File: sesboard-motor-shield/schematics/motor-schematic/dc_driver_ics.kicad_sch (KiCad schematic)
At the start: 0 parts

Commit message: added servo power supply
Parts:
- added J2: EXTERNAL_MOTOR_POWER, symbol Connector:Screw_Terminal_01x02
- added J3: MOTOR_C_OUT, symbol Connector:Screw_Terminal_01x02
- added J4: MOTOR_D_OUT, symbol Connector:Screw_Terminal_01x02
- added J5: MOTOR_A_OUT, symbol Connector:Screw_Terminal_01x02
- added J6: MOTOR_B_OUT, symbol Connector:Screw_Terminal_01x02
- added U2, U3: L293D, Package_DIP:DIP-16_W7.62mm, symbol Driver_Motor:L293D
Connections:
- new net +5V: U2.16 (VCC1), U3.16 (VCC1)
- new net ENA: U3.1 (EN1,2)
- new net ENB: U3.9 (EN3,4)
- new net ENC: U2.1 (EN1,2)
- new net END: U2.9 (EN3,4)
- new net GND: J2.1 (Pin_1), U2.12 (GND), U2.13 (GND), U2.4 (GND), U2.5 (GND), U3.12 (GND), U3.13 (GND), U3.4 (GND), U3.5 (GND)
- new net IN1: U3.2 (1A)
- new net IN2: U3.7 (2A)
- new net IN3: U3.10 (3A)
- new net IN4: U3.15 (4A)
- new net IN5: U2.2 (1A)
- new net IN6: U2.7 (2A)
- new net IN7: U2.10 (3A)
- new net IN8: U2.15 (4A)
- new net MOTOR_A_OUT+: J5.1 (Pin_1), U3.3 (1Y)
- new net MOTOR_A_OUT-: J5.2 (Pin_2), U3.6 (2Y)
- new net MOTOR_B_OUT-: J6.1 (Pin_1), J6.2 (Pin_2), U3.11 (3Y), U3.14 (4Y)
- new net MOTOR_C_OUT+: J3.1 (Pin_1), U2.3 (1Y)
- new net MOTOR_C_OUT-: J3.2 (Pin_2), U2.6 (2Y)
- new net MOTOR_D_OUT-: J4.1 (Pin_1), U2.11 (3Y), U2.14 (4Y)
- new net MOTOR_EXT+: J2.2 (Pin_2), U2.8 (VCC2), U3.8 (VCC2)
- new net MOTOR_d_OUT-: J4.2 (Pin_2)
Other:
- note added: "*a total of 4 DC motors can be controlled by these 2 ICs *a total of 2 stepper motors can be controlled by these 2 ICs"
- note added: "MOTOR DRIVERS"

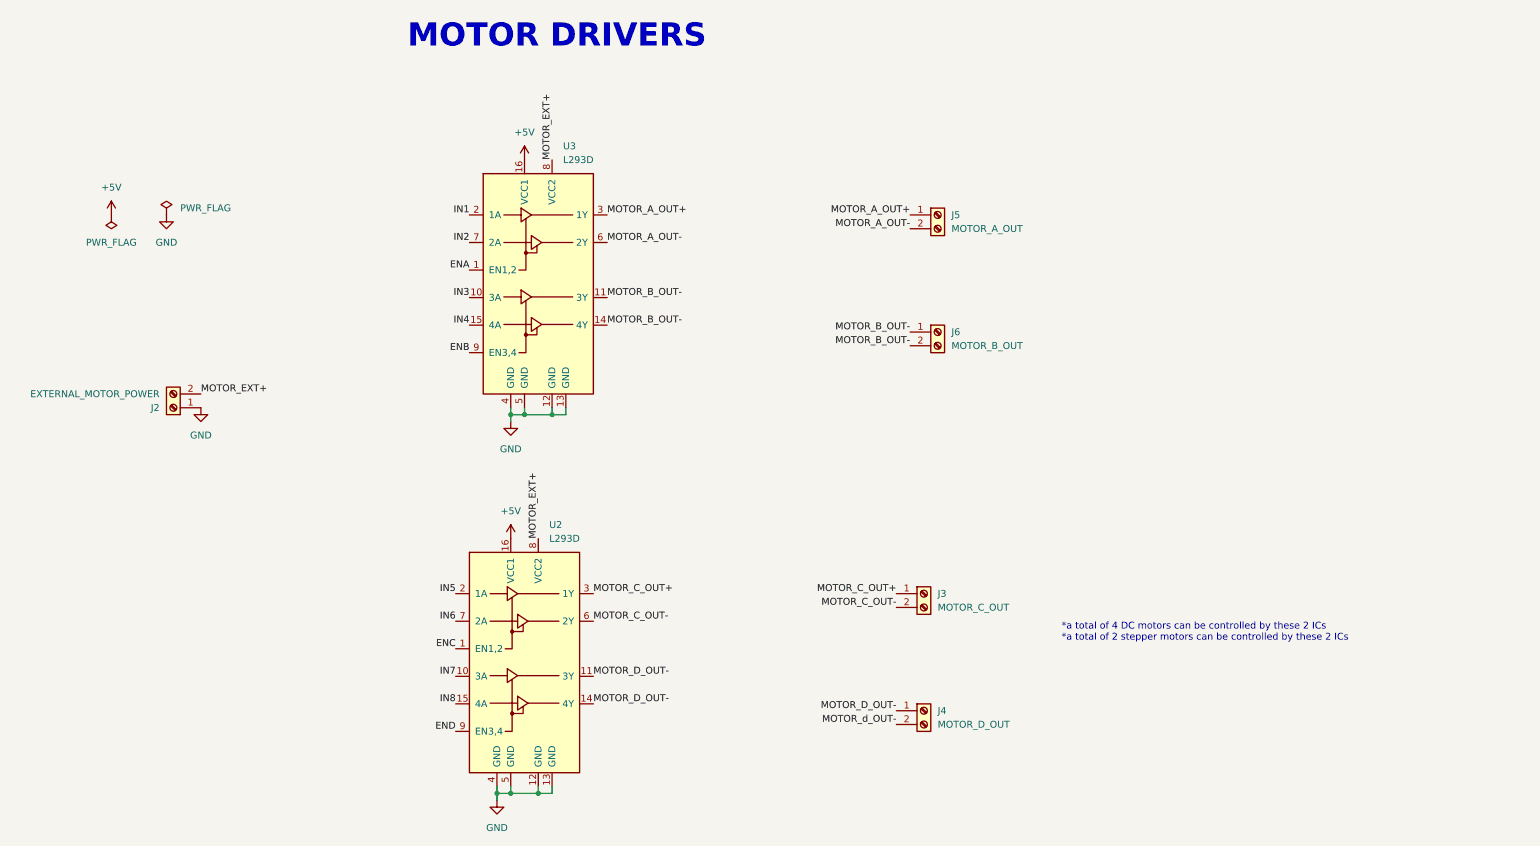
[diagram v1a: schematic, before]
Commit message: added pin assignments
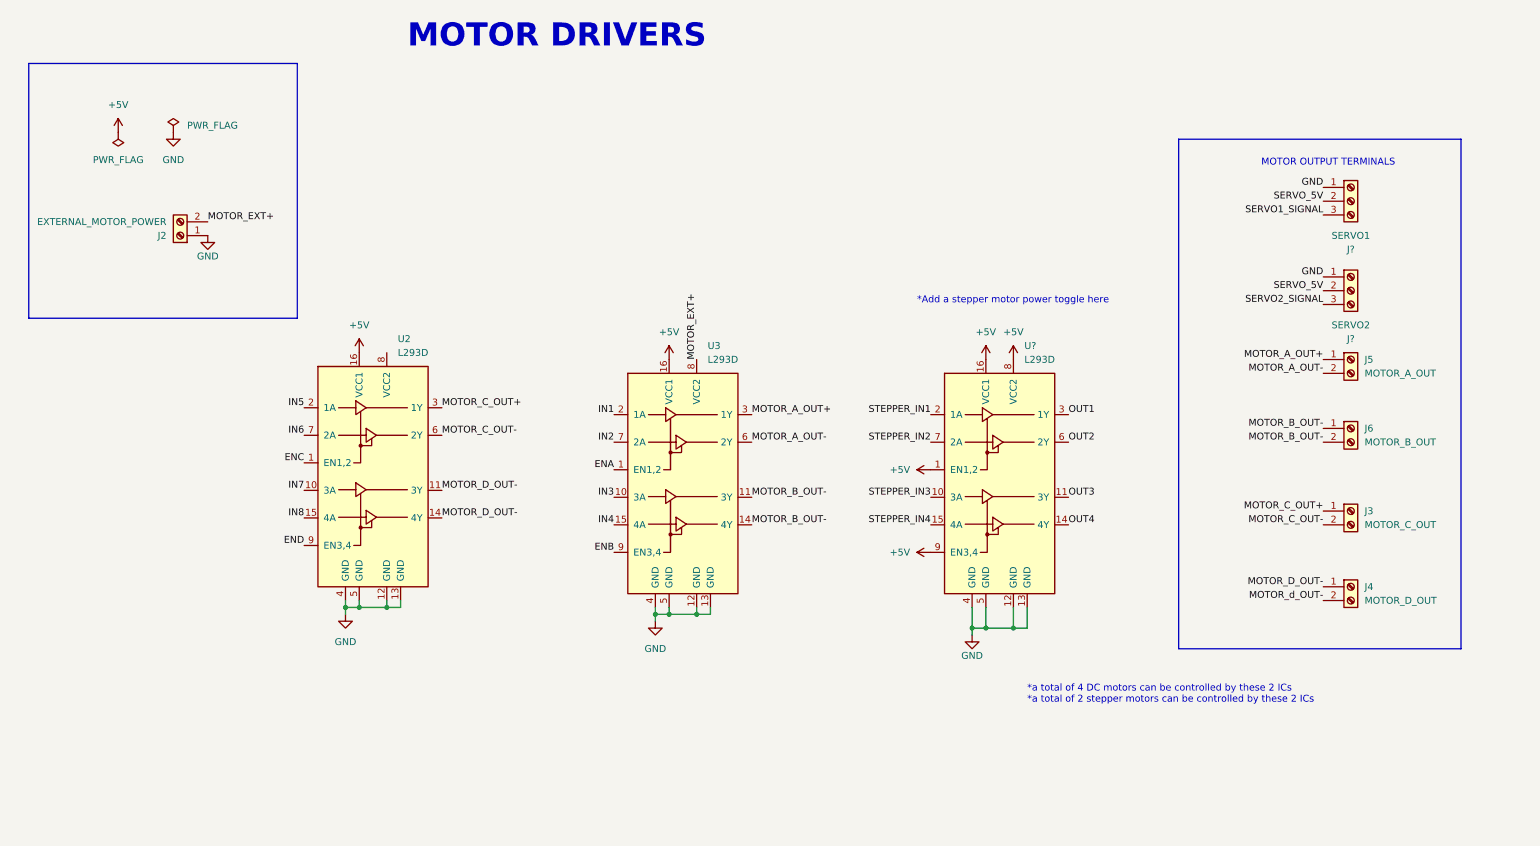
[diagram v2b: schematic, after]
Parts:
- added J?: SERVO2, symbol Connector:Screw_Terminal_01x03
- added J?: SERVO1, symbol Connector:Screw_Terminal_01x03
- added U?: L293D, Package_DIP:DIP-16_W7.62mm, symbol Driver_Motor:L293D
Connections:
- net +5V: now also U?.1 (EN1,2), U?.16 (VCC1), U?.8 (VCC2), U?.9 (EN3,4)
- net GND: now also J?.1 (Pin_1), J?.1 (Pin_1), U?.12 (GND), U?.13 (GND), U?.4 (GND), U?.5 (GND)
- net MOTOR_EXT+: no longer U2.8 (VCC2)
- new net OUT1: U?.3 (1Y)
- new net OUT2: U?.6 (2Y)
- new net OUT3: U?.11 (3Y)
- new net OUT4: U?.14 (4Y)
- new net SERVO1_SIGNAL: J?.3 (Pin_3)
- new net SERVO2_SIGNAL: J?.3 (Pin_3)
- new net SERVO_5V: J?.2 (Pin_2), J?.2 (Pin_2)
- new net STEPPER_IN1: U?.2 (1A)
- new net STEPPER_IN2: U?.7 (2A)
- new net STEPPER_IN3: U?.10 (3A)
- new net STEPPER_IN4: U?.15 (4A)
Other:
- note added: "*Add a stepper motor power toggle here"
- note added: "MOTOR OUTPUT TERMINALS"
- moved on the sheet: J2, J3, J4, J5, J6, U2, U3

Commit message: performed ERC
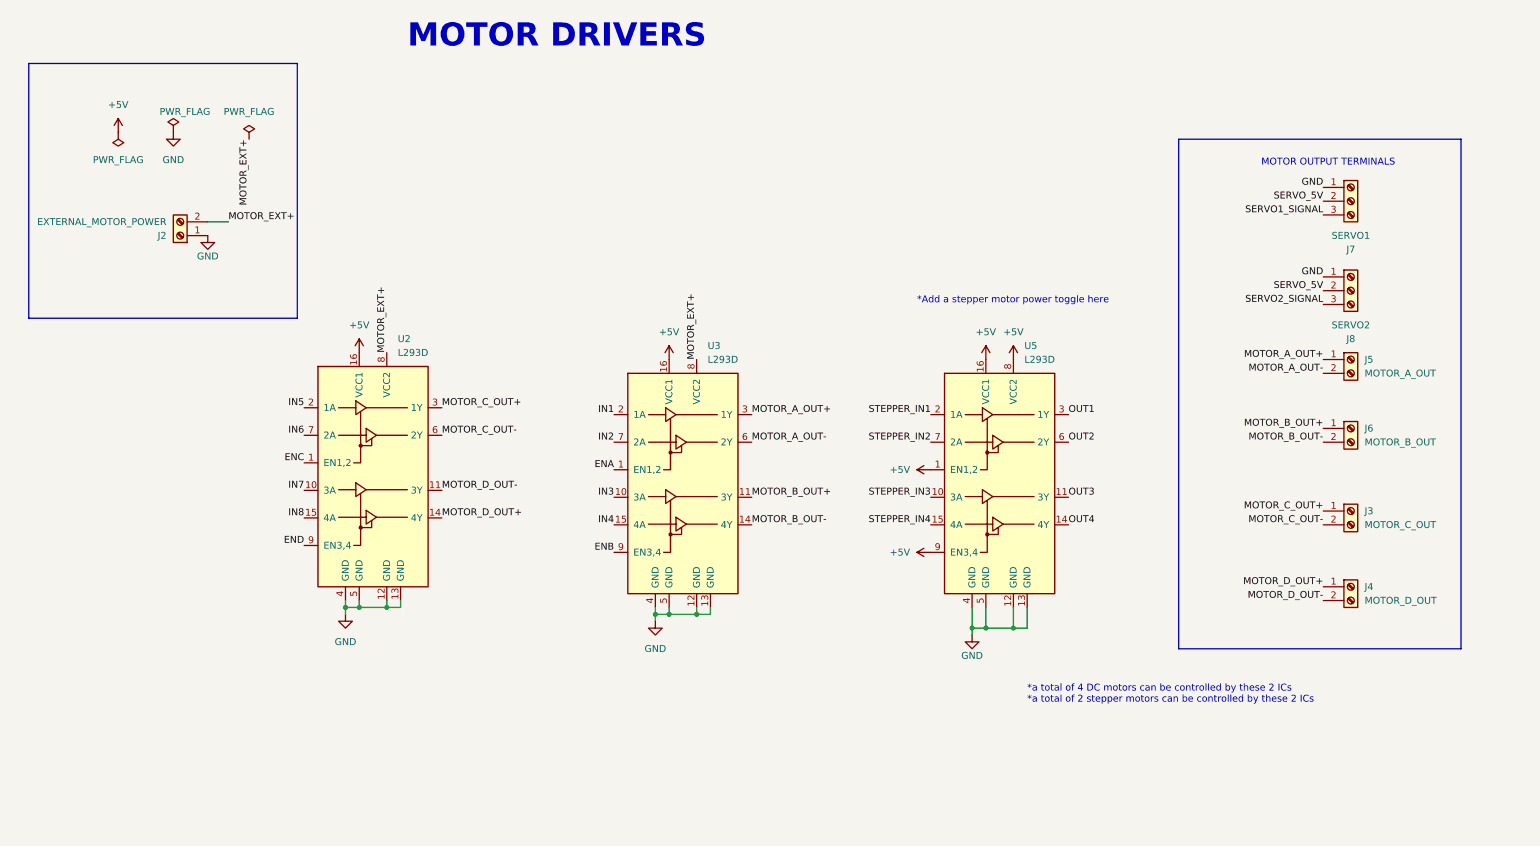
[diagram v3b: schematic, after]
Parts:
- gave numbers to parts that had none: 3
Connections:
- net MOTOR_d_OUT- is gone; now on net MOTOR_D_OUT-: J4.2 (Pin_2)
- net MOTOR_B_OUT-: no longer J6.1 (Pin_1), U3.11 (3Y)
- net MOTOR_D_OUT-: no longer J4.1 (Pin_1), U2.14 (4Y)
- net MOTOR_EXT+: now also U2.8 (VCC2)
- new net MOTOR_B_OUT+: J6.1 (Pin_1), U3.11 (3Y)
- new net MOTOR_D_OUT+: J4.1 (Pin_1), U2.14 (4Y)
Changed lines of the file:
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@@
+    (stroke (width 0) (type default) (color 0 0 0 0))
+  )
+  (wire (pts (xy 50.8 58.42) (xy 54.61 58.42))
     (stroke (width 0) (type default) (color 0 0 0 0))
   )
@@
     (effects (font (size 1.27 1.27)) (justify right bottom))
   )
-  (label "MOTOR_B_OUT-" (at 256.54 96.52 180)
+  (label "MOTOR_B_OUT+" (at 256.54 96.52 180)
     (effects (font (size 1.27 1.27)) (justify right bottom))
   )
@@
     (effects (font (size 1.27 1.27)) (justify right bottom))
   )
-  (label "MOTOR_D_OUT-" (at 256.54 125.73 180)
+  (label "MOTOR_D_OUT+" (at 256.54 125.73 180)
     (effects (font (size 1.27 1.27)) (justify right bottom))
   )
@@
     (effects (font (size 1.27 1.27)) (justify left bottom))
   )
-  (label "MOTOR_EXT+" (at 50.8 58.42 0)
-    (effects (font (size 1.27 1.27)) (justify left bottom))
-  )
-  (label "MOTOR_d_OUT-" (at 256.54 128.27 180)
+  (label "MOTOR_EXT+" (at 58.42 43.18 270)
+    (effects (font (size 1.27 1.27)) (justify right bottom))
+  )
+  (label "MOTOR_D_OUT-" (at 256.54 128.27 180)
     (effects (font (size 1.27 1.27)) (justify right bottom))
   )
@@
     (effects (font (size 1.27 1.27)) (justify right bottom))
   )
-  (label "MOTOR_B_OUT-" (at 151.13 109.22 0)
+  (label "MOTOR_B_OUT+" (at 151.13 109.22 0)
     (effects (font (size 1.27 1.27)) (justify left bottom))
   )
@@
     (effects (font (size 1.27 1.27)) (justify left bottom))
   )
-  (label "MOTOR_D_OUT-" (at 93.98 113.03 0)
+  (label "MOTOR_EXT+" (at 54.61 58.42 0)
+    (effects (font (size 1.27 1.27)) (justify left bottom))
+  )
+  (label "MOTOR_D_OUT+" (at 93.98 113.03 0)
     (effects (font (size 1.27 1.27)) (justify left bottom))
   )
@@
   (label "IN5" (at 68.58 92.71 180)
     (effects (font (size 1.27 1.27)) (justify right bottom))
+  )
+  (label "MOTOR_EXT+" (at 83.82 82.55 90)
+    (effects (font (size 1.27 1.27)) (justify left bottom))
   )
   (label "MOTOR_A_OUT+" (at 151.13 93.98 0)
@@
   (symbol (lib_id "power:GND") (at 191.77 134.62 0) (unit 1)
     (in_bom yes) (on_board yes)
-    (property "Reference" "#PWR?" (id 0) (at 191.77 140.97 0)
+    (property "Reference" "#PWR023" (id 0) (at 191.77 140.97 0)
       (effects (font (size 1.27 1.27)) hide)
     )
@@
   (symbol (lib_id "power:+5V") (at 194.31 83.82 0) (unit 1)
     (in_bom yes) (on_board yes) (fields_autoplaced)
-    (property "Reference" "#PWR?" (id 0) (at 194.31 87.63 0)
+    (property "Reference" "#PWR024" (id 0) (at 194.31 87.63 0)
       (effects (font (size 1.27 1.27)) hide)
     )
@@
   )
   (symbol (lib_id "power:PWR_FLAG") (at 44.45 41.91 0) (unit 1)
-    (in_bom yes) (on_board yes) (fields_autoplaced)
+    (in_bom yes) (on_board yes)
     (property "Reference" "#FLG02" (id 0) (at 44.45 40.005 0)
       (effects (font (size 1.27 1.27)) hide)
     )
-    (property "Value" "PWR_FLAG" (id 1) (at 46.99 40.6399 0)
+    (property "Value" "PWR_FLAG" (id 1) (at 41.91 38.1 0)
       (effects (font (size 1.27 1.27)) (justify left))
     )
@@
   (symbol (lib_id "power:+5V") (at 184.15 104.14 90) (unit 1)
     (in_bom yes) (on_board yes) (fields_autoplaced)
-    (property "Reference" "#PWR?" (id 0) (at 187.96 104.14 0)
+    (property "Reference" "#PWR021" (id 0) (at 187.96 104.14 0)
       (effects (font (size 1.27 1.27)) hide)
     )
@@
   (symbol (lib_id "Connector:Screw_Terminal_01x03") (at 261.62 71.12 0) (unit 1)
     (in_bom yes) (on_board yes) (fields_autoplaced)
-    (property "Reference" "J?" (id 0) (at 261.62 80.01 0))
+    (property "Reference" "J8" (id 0) (at 261.62 80.01 0))
     (property "Value" "SERVO2" (id 1) (at 261.62 77.47 0))
     (property "Footprint" "" (id 2) (at 261.62 71.12 0)
@@
   (symbol (lib_id "power:+5V") (at 184.15 119.38 90) (unit 1)
     (in_bom yes) (on_board yes) (fields_autoplaced)
-    (property "Reference" "#PWR?" (id 0) (at 187.96 119.38 0)
+    (property "Reference" "#PWR022" (id 0) (at 187.96 119.38 0)
       (effects (font (size 1.27 1.27)) hide)
     )
@@
   (symbol (lib_id "power:+5V") (at 199.39 83.82 0) (unit 1)
     (in_bom yes) (on_board yes) (fields_autoplaced)
-    (property "Reference" "#PWR?" (id 0) (at 199.39 87.63 0)
+    (property "Reference" "#PWR025" (id 0) (at 199.39 87.63 0)
       (effects (font (size 1.27 1.27)) hide)
     )
@@
     (pin "2")
   )
+  (symbol (lib_id "power:PWR_FLAG") (at 58.42 43.18 0) (unit 1)
+    (in_bom yes) (on_board yes) (fields_autoplaced)
+    (property "Reference" "#FLG0103" (id 0) (at 58.42 41.275 0)
+      (effects (font (size 1.27 1.27)) hide)
+    )
+    (property "Value" "PWR_FLAG" (id 1) (at 58.42 38.1 0))
+    (property "Footprint" "" (id 2) (at 58.42 43.18 0)
+      (effects (font (size 1.27 1.27)) hide)
+    )
+    (property "Datasheet" "~" (id 3) (at 58.42 43.18 0)
+      (effects (font (size 1.27 1.27)) hide)
+    )
+    (pin "1")
+  )
   (symbol (lib_id "Connector:Screw_Terminal_01x03") (at 261.62 54.61 0) (unit 1)
     (in_bom yes) (on_board yes) (fields_autoplaced)
-    (property "Reference" "J?" (id 0) (at 261.62 63.5 0))
+    (property "Reference" "J7" (id 0) (at 261.62 63.5 0))
     (property "Value" "SERVO1" (id 1) (at 261.62 60.96 0))
     (property "Footprint" "" (id 2) (at 261.62 54.61 0)
@@
   (symbol (lib_id "Driver_Motor:L293D") (at 196.85 109.22 0) (unit 1)
     (in_bom yes) (on_board yes) (fields_autoplaced)
-    (property "Reference" "U?" (id 0) (at 201.4094 81.28 0)
-      (effects (font (size 1.27 1.27)) (justify left))
-    )
+    (property "Reference" "U5" (id 0) (at 201.4094 81.28 0)
+      (effects (font (size 1.27 1.27)) (justify left))
+    )

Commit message: added global labels for motor drivers
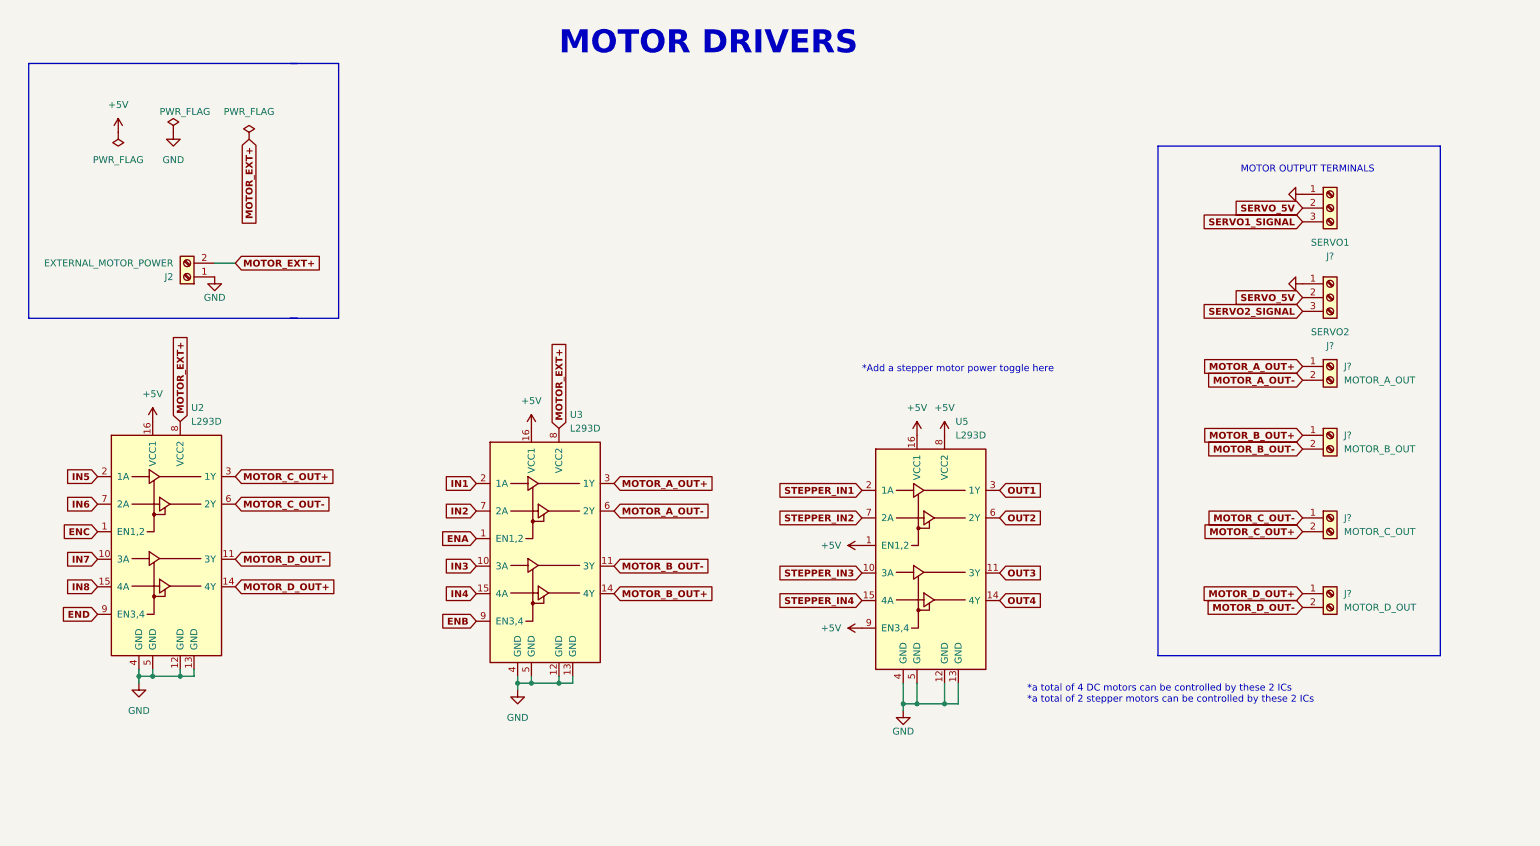
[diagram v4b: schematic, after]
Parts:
- removed J3: MOTOR_C_OUT, symbol Connector:Screw_Terminal_01x02
- removed J4: MOTOR_D_OUT, symbol Connector:Screw_Terminal_01x02
- removed J5: MOTOR_A_OUT, symbol Connector:Screw_Terminal_01x02
- removed J6: MOTOR_B_OUT, symbol Connector:Screw_Terminal_01x02
- removed J7: SERVO1, symbol Connector:Screw_Terminal_01x03
- removed J8: SERVO2, symbol Connector:Screw_Terminal_01x03
- added J?: MOTOR_C_OUT, TerminalBlock_Phoenix:TerminalBlock_Phoenix_MKDS-1,5-2_1x02_P5.00mm_Horizontal, symbol Connector:Screw_Terminal_01x02
- added J?: MOTOR_D_OUT, TerminalBlock_Phoenix:TerminalBlock_Phoenix_MKDS-1,5-2_1x02_P5.00mm_Horizontal, symbol Connector:Screw_Terminal_01x02
- added J?: MOTOR_A_OUT, TerminalBlock_Phoenix:TerminalBlock_Phoenix_MKDS-1,5-2_1x02_P5.00mm_Horizontal, symbol Connector:Screw_Terminal_01x02
- added J?: SERVO1, Connector_PinHeader_2.54mm:PinHeader_1x03_P2.54mm_Vertical, symbol Connector:Screw_Terminal_01x03
- added J?: MOTOR_B_OUT, TerminalBlock_Phoenix:TerminalBlock_Phoenix_MKDS-1,5-2_1x02_P5.00mm_Horizontal, symbol Connector:Screw_Terminal_01x02
- added J?: SERVO2, Connector_PinHeader_2.54mm:PinHeader_1x03_P2.54mm_Vertical, symbol Connector:Screw_Terminal_01x03
- J2: footprint (none) -> TerminalBlock_Phoenix:TerminalBlock_Phoenix_MKDS-1,5-2_1x02_P5.00mm_Horizontal
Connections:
- net GND: now also J?.1 (Pin_1), J?.1 (Pin_1)
- net MOTOR_A_OUT+: now also J?.1 (Pin_1)
- net MOTOR_A_OUT-: now also J?.2 (Pin_2)
- net MOTOR_B_OUT+: now also U3.14 (4Y), J?.1 (Pin_1); no longer U3.11 (3Y)
- net MOTOR_B_OUT-: now also U3.11 (3Y), J?.2 (Pin_2); no longer U3.14 (4Y)
- net MOTOR_C_OUT+: now also J?.2 (Pin_2)
- net MOTOR_C_OUT-: now also J?.1 (Pin_1)
- net MOTOR_D_OUT+: now also J?.1 (Pin_1)
- net MOTOR_D_OUT-: now also J?.2 (Pin_2)
- net SERVO1_SIGNAL: now also J?.3 (Pin_3)
- net SERVO2_SIGNAL: now also J?.3 (Pin_3)
- net SERVO_5V: now also J?.2 (Pin_2), J?.2 (Pin_2)
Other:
- title: (none) -> Motor Drivers
- moved on the sheet: J2, U2, U3, U5
